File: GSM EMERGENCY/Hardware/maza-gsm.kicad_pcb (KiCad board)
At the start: 2 copper layers, 0 parts

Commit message: Added the Accelerometer in sch.
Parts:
- added AE1: Antenna, kicad_libraries:GSM_ANTENNA_Yageo_ANT2112A010B0918A, F.Cu at (17.1, 99.7)
- added BT1: Battery_Cell, Pin_Headers:Pin_Header_Straight_1x02_Pitch2.54mm, F.Cu at (32.4, 188.0)
- added C1: 10pF, Capacitors_SMD:C_0805_HandSoldering, F.Cu at (19.0, 110.9)
- added C10: 10pF, Capacitors_SMD:C_0805_HandSoldering, F.Cu at (19.3, 139.0)
- added C11: 10pF, Capacitors_SMD:C_0805_HandSoldering, F.Cu at (19.2, 141.9)
- added C12: 10pF, Capacitors_SMD:C_0805_HandSoldering, F.Cu at (19.3, 144.8)
- added C13: 470uF,E, Capacitors_SMD:CP_Elec_10x10.5, F.Cu at (70.8, 173.3)
- added C14: 33pF, Capacitors_SMD:C_0805_HandSoldering, F.Cu at (24.8, 33.7)
- added C15: 33pF, Capacitors_SMD:C_0805_HandSoldering, F.Cu at (26.0, 111.4)
- added C16: 33pF, Capacitors_SMD:C_0805_HandSoldering, F.Cu at (25.9, 113.7)
- added C17: 33pF, Capacitors_SMD:C_0805_HandSoldering, F.Cu at (26.0, 116.2)
- added C18: 33pF, Capacitors_SMD:C_0805_HandSoldering, F.Cu at (26.0, 118.9)
- added C19: 33pF, Capacitors_SMD:C_0805_HandSoldering, F.Cu at (25.9, 122.1)
- added C2: 10pF, Capacitors_SMD:C_0805_HandSoldering, F.Cu at (18.8, 113.9)
- added C20: 33pF, Capacitors_SMD:C_0805_HandSoldering, F.Cu at (25.5, 125.2)
- added C21: 33pF, Capacitors_SMD:C_0805_HandSoldering, F.Cu at (26.0, 128.8)
- added C22: 33pF, Capacitors_SMD:C_0805_HandSoldering, F.Cu at (26.1, 132.2)
- added C23: 33pF, Capacitors_SMD:C_0805_HandSoldering, F.Cu at (26.0, 136.3)
- added C24: 33pF, Capacitors_SMD:C_0805_HandSoldering, F.Cu at (26.3, 139.2)
- added C25: 33pF, Capacitors_SMD:C_0805_HandSoldering, F.Cu at (26.9, 141.7)
- added C26: 33pF, Capacitors_SMD:C_0805_HandSoldering, F.Cu at (27.3, 144.9)
- added C27: 100nF, Capacitors_SMD:C_0805_HandSoldering, F.Cu at (87.7, 192.3)
- added C28: 33pF, Capacitors_SMD:C_0805_HandSoldering, F.Cu at (31.4, 34.2)
- added C29: 33pF, Capacitors_SMD:C_0805_HandSoldering, F.Cu at (25.3, 36.9)
- added C3: 10pF, Capacitors_SMD:C_0805_HandSoldering, F.Cu at (18.6, 117.5)
- added C30: 33pF, Capacitors_SMD:C_0805_HandSoldering, F.Cu at (38.6, 19.2)
- added C31: 470uF,E, Capacitors_SMD:CP_Elec_10x10.5, F.Cu at (68.9, 185.3)
- added C32: 100nF, Capacitors_SMD:C_0805_HandSoldering, F.Cu at (84.5, 171.4)
- added C33: 100uF,Tantalum, ESR=0.7Ohm, Capacitors_Tantalum_SMD:CP_Tantalum_Case-X_EIA-7343-43_Hand, F.Cu at (90.7, 186.7)
- added C34: 100nF, Capacitors_SMD:C_0805_HandSoldering, F.Cu at (37.6, 35.8)
- added C35: 100nF, Capacitors_SMD:C_0805_HandSoldering, F.Cu at (86.9, 175.3)
- added C36: 100nF, Capacitors_SMD:C_0805_HandSoldering, F.Cu at (38.6, 15.0)
- added C37: 10pF, Capacitors_SMD:C_0805_HandSoldering, F.Cu at (86.9, 178.6)
- added C38: 33pF, Capacitors_SMD:C_0805_HandSoldering, F.Cu at (86.9, 181.3)
- added C39: 10pF, Capacitors_SMD:C_0805_HandSoldering, F.Cu at (49.7, 110.6)
- added C4: 10pF, Capacitors_SMD:C_0805_HandSoldering, F.Cu at (18.6, 119.7)
- added C40: 10pF, Capacitors_SMD:C_0805_HandSoldering, F.Cu at (50.2, 113.2)
- added C41: 10pF, Capacitors_SMD:C_0805_HandSoldering, F.Cu at (50.0, 115.8)
- added C42: 22uF, Capacitors_SMD:C_0805_HandSoldering, F.Cu at (50.0, 118.2)
- added C43: 33pF, Capacitors_SMD:C_0805_HandSoldering, F.Cu at (57.0, 110.4)
- added C44: 33pF, Capacitors_SMD:C_0805_HandSoldering, F.Cu at (57.1, 113.1)
- added C45: 33pF, Capacitors_SMD:C_0805_HandSoldering, F.Cu at (57.2, 115.8)
- added C46: 10uF, Capacitors_SMD:C_0805_HandSoldering, F.Cu at (57.6, 118.6)
- added C47: 33pF, Capacitors_SMD:C_0805_HandSoldering, F.Cu at (57.9, 121.2)
- added C48: 1uF, Capacitors_SMD:C_0805_HandSoldering, F.Cu at (155.0, 171.1)
- added C49: NM C, Capacitors_SMD:C_0805_HandSoldering, F.Cu at (27.7, 103.0)
- added C5: 10pF, Capacitors_SMD:C_0805_HandSoldering, F.Cu at (18.9, 123.7)
- added C50: NM C, Capacitors_SMD:C_0805_HandSoldering, F.Cu at (93.8, 108.6)
- added C51: NM C, Capacitors_SMD:C_0805_HandSoldering, F.Cu at (94.4, 111.7)
- added C52: 10uF, Capacitors_SMD:C_0805_HandSoldering, F.Cu at (51.8, 123.9)
- added C53: 4.7uF, Capacitors_SMD:C_0805_HandSoldering, F.Cu at (51.4, 121.0)
- added C54: 33pF, Capacitors_SMD:C_0805_HandSoldering, F.Cu at (57.6, 123.8)
- added C55: 33pF, Capacitors_SMD:C_0805_HandSoldering, F.Cu at (58.0, 32.4)
- added C56: NM C, Capacitors_SMD:C_0805_HandSoldering, F.Cu at (33.1, 103.1)
- added C57: NM C, Capacitors_SMD:C_0805_HandSoldering, F.Cu at (93.7, 105.4)
- added C58: NM C, Capacitors_SMD:C_0805_HandSoldering, F.Cu at (94.6, 115.2)
- added C59: 33pF, Capacitors_SMD:C_0805_HandSoldering, F.Cu at (63.8, 32.3)
- added C6: 10pF, Capacitors_SMD:C_0805_HandSoldering, F.Cu at (18.9, 126.5)
- added C60: 33pF, Capacitors_SMD:C_0805_HandSoldering, F.Cu at (59.2, 35.3)
- added C61: 4.7uF, Capacitors_SMD:C_0805_HandSoldering, F.Cu at (155.4, 174.7)
- added C62: 33pF, Capacitors_SMD:C_0805_HandSoldering, F.Cu at (64.3, 35.6)
- added C63: 100nF, Capacitors_SMD:C_0805_HandSoldering, F.Cu at (155.4, 178.2)
- added C64: 10uF, Capacitors_SMD:C_0805_HandSoldering, F.Cu at (155.5, 184.8)
- added C65: 100nF, Capacitors_SMD:C_0805_HandSoldering, F.Cu at (155.5, 181.6)
- added C66: 100nF, Capacitors_SMD:C_0805_HandSoldering, F.Cu at (67.9, 26.3)
- added C67: 100nF, Capacitors_SMD:C_0805_HandSoldering, F.Cu at (68.0, 29.3)
- added C68: 100uF, Capacitors_SMD:C_0805_HandSoldering, F.Cu at (16.9, 167.7)
- added C69: 4.7uF, Capacitors_SMD:C_0805_HandSoldering, F.Cu at (13.6, 167.6)
- added C7: 10pF, Capacitors_SMD:C_0805_HandSoldering, F.Cu at (19.1, 129.4)
- added C70: 100uF, Capacitors_SMD:C_0805_HandSoldering, F.Cu at (20.5, 167.7)
- added C71: 100uF, Capacitors_SMD:C_0805_HandSoldering, F.Cu at (24.6, 167.8)
- added C72: 100uF, Capacitors_SMD:C_0805_HandSoldering, F.Cu at (27.7, 167.8)
- added C73: 0.1uF, Capacitors_SMD:C_0805_HandSoldering, F.Cu at (111.3, 102.9)
- added C74: 15pF, Capacitors_SMD:C_0805_HandSoldering, F.Cu at (121.3, 105.9)
- added C75: 4.7uF, Capacitors_SMD:C_0805_HandSoldering, F.Cu at (25.7, 174.2)
- added C76: 0.1uF, Capacitors_SMD:C_0805_HandSoldering, F.Cu at (25.3, 182.4)
- added C77: 1uF, Capacitors_SMD:C_0805_HandSoldering, F.Cu at (24.7, 190.7)
- added C78: 0.15uF, Capacitors_SMD:C_0805_HandSoldering, F.Cu at (24.7, 187.6)
- added C79: 10uF, Capacitors_SMD:C_0805_HandSoldering, F.Cu at (42.9, 185.8)
- added C8: 10pF, Capacitors_SMD:C_0805_HandSoldering, F.Cu at (19.0, 132.8)
- added C80: 10uF, Capacitors_SMD:C_0805_HandSoldering, F.Cu at (36.5, 188.0)
- added C81: 0.47uF, Capacitors_SMD:C_0805_HandSoldering, F.Cu at (93.5, 140.9)
- added C82: 33uF, Capacitors_SMD:C_0805_HandSoldering, F.Cu at (93.6, 137.8)
- added C83: 47pF, Capacitors_SMD:C_0805_HandSoldering, F.Cu at (125.6, 38.2)
- added C84: 1pF, Capacitors_SMD:C_0805_HandSoldering, F.Cu at (125.5, 41.9)
- added C85: 33uF,16V, Capacitors_SMD:CP_Elec_3x5.3, F.Cu at (115.0, 42.1)
- added C86: CP10uF,Tantalum, ESR=0.7Ohm, Capacitors_Tantalum_SMD:CP_Tantalum_Case-A_EIA-3216-18_Hand, F.Cu at (132.4, 79.6)
- added C87: 33uF,16V,E, Capacitors_SMD:CP_Elec_3x5.3, F.Cu at (113.6, 34.8)
- added C88: 4.7uF,16V,E, Capacitors_SMD:CP_Elec_4x5.3, F.Cu at (106.1, 17.7)
- added C89: 4.7uF, Capacitors_SMD:C_0805_HandSoldering, F.Cu at (112.4, 16.3)
- added C9: 10pF, Capacitors_SMD:C_0805_HandSoldering, F.Cu at (19.3, 136.5)
- added C90: 4.7uF, Capacitors_SMD:C_0805_HandSoldering, F.Cu at (112.3, 19.9)
- added C91: 10uF,16V,E, Capacitors_SMD:CP_Elec_5x5.3, F.Cu at (104.4, 26.3)
- added D1: TVS_DIODE_CM1224, kicad_libraries:CM1224-4SO-SOT23, F.Cu at (19.5, 35.8)
- added D10: TVS_DIODE_CM1224, kicad_libraries:CM1224-4SO-SOT23, F.Cu at (51.7, 33.3)
- added D11: D_TVS_ALT, Diodes_SMD:D_SOD-123, F.Cu at (63.3, 122.3)
- added D12: SS14FL, kicad_libraries:SChottky-diode-SS14FL-Fairchild, F.Cu at (107.1, 31.9)
- added D2: ESD, Diodes_SMD:D_SOD-123, F.Cu at (35.3, 119.3)
- added D3: ESD, Diodes_SMD:D_SOD-123, F.Cu at (35.4, 122.7)
- added D4: ESD, Diodes_SMD:D_SOD-123, F.Cu at (35.7, 126.2)
- added D5: ESD, Diodes_SMD:D_SOD-123, F.Cu at (36.1, 129.9)
- added D6: ESD, Diodes_SMD:D_SOD-123, F.Cu at (35.9, 133.6)
- added D7: ESD, Diodes_SMD:D_SOD-123, F.Cu at (36.0, 137.2)
- added D8: 5.1V Zener, Diodes_SMD:D_SOD-123, F.Cu at (93.3, 175.9)
- added D9: D_TVS_ALT, Diodes_SMD:D_SOD-123, F.Cu at (50.1, 130.1)
- added F1: IPEX_CON, kicad_libraries:IPEX_CON_MHF, F.Cu at (87.7, 112.3)
- added F2: IPEX_CON, kicad_libraries:IPEX_CON_MHF, F.Cu at (82.2, 112.2)
- added J1: SIM_Card, kicad_libraries:MICRO-SIM-78646-3001-MOLEX, F.Cu at (30.7, 29.3)
- added J10: ON_OFF_SWITCH, Connectors_Terminal_Blocks:TerminalBlock_Pheonix_MPT-2.54mm_3pol, F.Cu at (33.7, 172.9)
- added J11: LED2, Connectors_Terminal_Blocks:TerminalBlock_Pheonix_MPT-2.54mm_2pol, F.Cu at (106.2, 125.1)
- added J12: LED3, Connectors_Terminal_Blocks:TerminalBlock_Pheonix_MPT-2.54mm_2pol, F.Cu at (106.3, 137.0)
- added J13: LED4, Connectors_Terminal_Blocks:TerminalBlock_Pheonix_MPT-2.54mm_2pol, F.Cu at (106.5, 148.2)
- added J14: LED5, Connectors_Terminal_Blocks:TerminalBlock_Pheonix_MPT-2.54mm_2pol, F.Cu at (107.3, 159.1)
- added J15: LED6, Connectors_Terminal_Blocks:TerminalBlock_Pheonix_MPT-2.54mm_2pol, F.Cu at (107.3, 169.3)
- added J16: LED7, Connectors_Terminal_Blocks:TerminalBlock_Pheonix_MPT-2.54mm_2pol, F.Cu at (107.7, 180.2)
- added J17: LED8, Connectors_Terminal_Blocks:TerminalBlock_Pheonix_MPT-2.54mm_2pol, F.Cu at (109.0, 190.3)
- added J18: OLED CONNECTOR, Connectors_Molex:Molex_Panelmate-53780-3070_30x1.25mm_Angled, F.Cu at (142.0, 37.3)
- added J19: PB1, Pin_Headers:Pin_Header_Straight_1x02_Pitch2.54mm, F.Cu at (93.2, 17.9)
- added J2: NETWORK_LED, Connectors_Terminal_Blocks:TerminalBlock_Pheonix_MPT-2.54mm_2pol, F.Cu at (34.1, 52.6)
- added J20: PB2, Pin_Headers:Pin_Header_Straight_1x02_Pitch2.54mm, F.Cu at (86.7, 17.9)
- added J21: PB3, Pin_Headers:Pin_Header_Straight_1x02_Pitch2.54mm, F.Cu at (82.2, 17.3)
- added J22: PB4, Pin_Headers:Pin_Header_Straight_1x02_Pitch2.54mm, F.Cu at (77.5, 17.5)
- added J23: OLED_INDICATOR, Pin_Headers:Pin_Header_Straight_1x02_Pitch2.54mm, F.Cu at (127.1, 17.9)
- added J24: 32Ohm,Speaker, Pin_Headers:Pin_Header_Straight_1x02_Pitch2.54mm, F.Cu at (41.1, 120.0)
- added J25: 8OHM, SPEAKER, Pin_Headers:Pin_Header_Straight_1x02_Pitch2.54mm, F.Cu at (41.3, 130.0)
- added J26: 2.2Kohms, Load Res.Mic, Pin_Headers:Pin_Header_Straight_1x02_Pitch2.54mm, F.Cu at (41.1, 138.8)
- added J27: ICSP, Pin_Headers:Pin_Header_Straight_1x05_Pitch2.54mm, F.Cu at (99.2, 80.8)
- added J3: PCM CON, Pin_Headers:Pin_Header_Straight_1x04_Pitch2.54mm, F.Cu at (19.7, 73.4)
- added J4: SD CON, Pin_Headers:Pin_Header_Straight_1x03_Pitch2.54mm, F.Cu at (40.3, 69.2)
- added J5: 1PPS_LED, Connectors_Terminal_Blocks:TerminalBlock_Pheonix_MPT-2.54mm_2pol, F.Cu at (67.7, 86.0)
- added J6: SIM_Card, kicad_libraries:MICRO-SIM-78646-3001-MOLEX, F.Cu at (63.2, 27.9)
- added J7: USB_OTG, Connectors:USB_Micro-B_10103594-0001LF, F.Cu at (16.9, 189.2)
- added J8: POWER_ADAPTER, Connectors_Terminal_Blocks:TerminalBlock_Pheonix_MPT-2.54mm_2pol, F.Cu at (16.2, 178.5)
- added J9: LED1, Connectors_Terminal_Blocks:TerminalBlock_Pheonix_MPT-2.54mm_2pol, F.Cu at (110.0, 119.0)
- added L1: 1uH, Inductors_SMD:L_0805_HandSoldering, F.Cu at (42.4, 181.5)
- added L2: 18uH, Inductors_SMD:L_0805_HandSoldering, F.Cu at (106.5, 35.9)
- added Q1: BC847, TO_SOT_Packages_SMD:SOT-23_Handsoldering, F.Cu at (27.0, 54.6)
- added Q10: BC847, TO_SOT_Packages_SMD:SOT-23_Handsoldering, F.Cu at (124.0, 53.0)
- added Q11: BC847, TO_SOT_Packages_SMD:SOT-23_Handsoldering, F.Cu at (117.0, 167.8)
- added Q12: BC847, TO_SOT_Packages_SMD:SOT-23_Handsoldering, F.Cu at (116.2, 179.2)
- added Q13: BC847, TO_SOT_Packages_SMD:SOT-23_Handsoldering, F.Cu at (116.5, 191.1)
- added Q2: BC847, TO_SOT_Packages_SMD:SOT-23_Handsoldering, F.Cu at (81.0, 176.4)
- added Q3: BC857, TO_SOT_Packages_SMD:SOT-23_Handsoldering, F.Cu at (54.9, 87.9)
- added Q4: BC847, TO_SOT_Packages_SMD:SOT-23_Handsoldering, F.Cu at (90.3, 151.0)
- added Q5: BC847, TO_SOT_Packages_SMD:SOT-23_Handsoldering, F.Cu at (117.8, 117.0)
- added Q6: BC847, TO_SOT_Packages_SMD:SOT-23_Handsoldering, F.Cu at (117.5, 126.9)
- added Q7: BC847, TO_SOT_Packages_SMD:SOT-23_Handsoldering, F.Cu at (118.0, 136.1)
- added Q8: BC847, TO_SOT_Packages_SMD:SOT-23_Handsoldering, F.Cu at (117.7, 146.8)
- added Q9: BC847, TO_SOT_Packages_SMD:SOT-23_Handsoldering, F.Cu at (117.2, 158.8)
- added R1: 0R, Resistors_SMD:R_0805_HandSoldering, F.Cu at (31.5, 111.8)
- added R10: 300R, Resistors_SMD:R_0805_HandSoldering, F.Cu at (22.2, 52.4)
- added R11: 0R, Resistors_SMD:R_0805_HandSoldering, F.Cu at (35.3, 141.0)
- added R12: 0R, Resistors_SMD:R_0805_HandSoldering, F.Cu at (34.6, 144.6)
- added R13: 124K, Resistors_SMD:R_0805_HandSoldering, F.Cu at (78.1, 189.6)
- added R14: 56K, Resistors_SMD:R_0805_HandSoldering, F.Cu at (78.1, 183.3)
- added R15: 470R, Resistors_SMD:R_0805_HandSoldering, F.Cu at (77.6, 186.4)
- added R16: 22R, Resistors_SMD:R_0805_HandSoldering, F.Cu at (38.0, 31.1)
- added R17: 22R, Resistors_SMD:R_0805_HandSoldering, F.Cu at (38.1, 27.3)
- added R18: 22R, Resistors_SMD:R_0805_HandSoldering, F.Cu at (38.1, 23.5)
- added R19: 4.7K, Resistors_SMD:R_0805_HandSoldering, F.Cu at (60.6, 83.1)
- added R2: 0R, Resistors_SMD:R_0805_HandSoldering, F.Cu at (32.2, 114.7)
- added R20: 0R, Resistors_SMD:R_0805_HandSoldering, F.Cu at (63.0, 109.9)
- added R21: 0R, Resistors_SMD:R_0805_HandSoldering, F.Cu at (62.9, 113.3)
- added R22: 0R, Resistors_SMD:R_0805_HandSoldering, F.Cu at (63.0, 116.3)
- added R23: 47K, Resistors_SMD:R_0805_HandSoldering, F.Cu at (60.8, 86.8)
- added R24: 300R, Resistors_SMD:R_0805_HandSoldering, F.Cu at (61.2, 91.0)
- added R25: 0R, Resistors_SMD:R_0805_HandSoldering, F.Cu at (73.6, 55.2)
- added R26: 0R, Resistors_SMD:R_0805_HandSoldering, F.Cu at (72.9, 59.1)
- added R27: 47K, Resistors_SMD:R_0805_HandSoldering, F.Cu at (162.4, 174.8)
- added R28: 0R, Resistors_SMD:R_0805_HandSoldering, F.Cu at (20.4, 102.8)
- added R29: 0R, Resistors_SMD:R_0805_HandSoldering, F.Cu at (82.4, 106.9)
- added R3: 4.7K, Resistors_SMD:R_0805_HandSoldering, F.Cu at (21.9, 49.4)
- added R30: 0R, Resistors_SMD:R_0805_HandSoldering, F.Cu at (88.3, 106.7)
- added R31: 1K, Resistors_SMD:R_0805_HandSoldering, F.Cu at (73.0, 64.6)
- added R32: 1K, Resistors_SMD:R_0805_HandSoldering, F.Cu at (73.0, 67.4)
- added R33: 1K, Resistors_SMD:R_0805_HandSoldering, F.Cu at (73.1, 69.8)
- added R34: 1K, Resistors_SMD:R_0805_HandSoldering, F.Cu at (73.5, 72.4)
- added R35: 5.6K, Resistors_SMD:R_0805_HandSoldering, F.Cu at (73.9, 61.6)
- added R36: 75K, 1%, Resistors_SMD:R_0805_HandSoldering, F.Cu at (162.7, 178.8)
- added R37: 43K, 1%, Resistors_SMD:R_0805_HandSoldering, F.Cu at (162.6, 183.1)
- added R38: 22R, Resistors_SMD:R_0805_HandSoldering, F.Cu at (68.1, 23.5)
- added R39: 22R, Resistors_SMD:R_0805_HandSoldering, F.Cu at (67.5, 19.5)
- added R4: 4.7K, Resistors_SMD:R_0805_HandSoldering, F.Cu at (96.0, 191.5)
- added R40: 22R, Resistors_SMD:R_0805_HandSoldering, F.Cu at (67.3, 15.5)
- added R41: 4.7K, Resistors_SMD:R_0805_HandSoldering, F.Cu at (91.8, 155.6)
- added R42: 47K, Resistors_SMD:R_0805_HandSoldering, F.Cu at (95.8, 150.8)
- added R43: 10K, Resistors_SMD:R_0805_HandSoldering, F.Cu at (89.1, 24.3)
- added R44: 0R, Resistors_SMD:R_0805_HandSoldering, F.Cu at (82.8, 25.8)
- added R45: 10K, Resistors_SMD:R_0805_HandSoldering, F.Cu at (88.5, 28.3)
- added R46: 10K, Resistors_SMD:R_0805_HandSoldering, F.Cu at (111.4, 99.0)
- added R47: 0R, Resistors_SMD:R_0805_HandSoldering, F.Cu at (25.3, 178.5)
- added R48: 0R, Resistors_SMD:R_0805_HandSoldering, F.Cu at (81.7, 29.6)
- added R49: 10K, Resistors_SMD:R_0805_HandSoldering, F.Cu at (81.5, 33.1)
- added R5: 47K, Resistors_SMD:R_0805_HandSoldering, F.Cu at (96.5, 195.5)
- added R50: 0R, Resistors_SMD:R_0805_HandSoldering, F.Cu at (82.0, 36.4)
- added R51: 100K, Resistors_SMD:R_0805_HandSoldering, F.Cu at (43.1, 189.5)
- added R52: 100K, Resistors_SMD:R_0805_HandSoldering, F.Cu at (37.5, 184.1)
- added R53: 10K, Resistors_SMD:R_0805_HandSoldering, F.Cu at (88.2, 32.7)
- added R54: 3K, Resistors_SMD:R_0805_HandSoldering, F.Cu at (38.7, 178.7)
- added R55: 0R, Resistors_SMD:R_0805_HandSoldering, F.Cu at (88.8, 36.9)
- added R56: 1.2K, Resistors_SMD:R_0805_HandSoldering, F.Cu at (39.0, 192.3)
- added R57: 100K, Resistors_SMD:R_0805_HandSoldering, F.Cu at (42.4, 178.0)
- added R58: 4.7K, Resistors_SMD:R_0805_HandSoldering, F.Cu at (121.3, 117.0)
- added R59: 100K, Resistors_SMD:R_0805_HandSoldering, F.Cu at (42.0, 174.2)
- added R6: 0R, Resistors_SMD:R_0805_HandSoldering, F.Cu at (40.1, 111.7)
- added R60: 47K, Resistors_SMD:R_0805_HandSoldering, F.Cu at (128.9, 117.0)
- added R61: 300R, Resistors_SMD:R_0805_HandSoldering, F.Cu at (124.6, 117.2)
- added R62: 4.7K, Resistors_SMD:R_0805_HandSoldering, F.Cu at (125.0, 127.7)
- added R63: 47K, Resistors_SMD:R_0805_HandSoldering, F.Cu at (128.3, 127.0)
- added R64: 300R, Resistors_SMD:R_0805_HandSoldering, F.Cu at (121.9, 126.7)
- added R65: 4.7K, Resistors_SMD:R_0805_HandSoldering, F.Cu at (121.7, 136.1)
- added R66: 47K, Resistors_SMD:R_0805_HandSoldering, F.Cu at (125.0, 136.4)
- added R67: 300R, Resistors_SMD:R_0805_HandSoldering, F.Cu at (128.7, 136.7)
- added R68: 4.7K, Resistors_SMD:R_0805_HandSoldering, F.Cu at (122.0, 146.7)
- added R69: 10K, Resistors_SMD:R_0805_HandSoldering, F.Cu at (119.6, 31.6)
- added R7: 0R, Resistors_SMD:R_0805_HandSoldering, F.Cu at (40.1, 114.5)
- added R70: 47K, Resistors_SMD:R_0805_HandSoldering, F.Cu at (124.9, 147.1)
- added R71: 300R, Resistors_SMD:R_0805_HandSoldering, F.Cu at (129.4, 146.8)
- added R72: 4.7K, Resistors_SMD:R_0805_HandSoldering, F.Cu at (125.2, 160.3)
- added R73: 47K, Resistors_SMD:R_0805_HandSoldering, F.Cu at (129.1, 159.9)
- added R74: 4.7K, Resistors_SMD:R_0805_HandSoldering, F.Cu at (128.4, 46.2)
- added R75: 300R, Resistors_SMD:R_0805_HandSoldering, F.Cu at (122.0, 159.7)
- added R76: 300R, Resistors_SMD:R_0805_HandSoldering, F.Cu at (123.5, 46.5)
- added R77: 4.7K, Resistors_SMD:R_0805_HandSoldering, F.Cu at (121.4, 168.6)
- added R78: 47K, Resistors_SMD:R_0805_HandSoldering, F.Cu at (124.8, 168.3)
- added R79: 300R, Resistors_SMD:R_0805_HandSoldering, F.Cu at (129.2, 169.0)
- added R8: 51K, Resistors_SMD:R_0805_HandSoldering, F.Cu at (90.5, 195.8)
- added R80: 3K3, Resistors_SMD:R_0805_HandSoldering, F.Cu at (131.9, 20.6)
- added R81: 4.7K, Resistors_SMD:R_0805_HandSoldering, F.Cu at (120.8, 179.0)
- added R82: 47K, Resistors_SMD:R_0805_HandSoldering, F.Cu at (124.0, 179.1)
- added R83: 300R, Resistors_SMD:R_0805_HandSoldering, F.Cu at (128.0, 179.4)
- added R84: 0R, Resistors_SMD:R_0805_HandSoldering, F.Cu at (128.4, 85.5)
- added R85: 4.7K, Resistors_SMD:R_0805_HandSoldering, F.Cu at (121.2, 190.9)
- added R86: 820K, Resistors_SMD:R_0805_HandSoldering, F.Cu at (112.7, 31.1)
- added R87: 47K, Resistors_SMD:R_0805_HandSoldering, F.Cu at (125.6, 191.1)
- added R88: 0R, Resistors_SMD:R_0805_HandSoldering, F.Cu at (133.8, 84.1)
- added R89: 300R, Resistors_SMD:R_0805_HandSoldering, F.Cu at (130.0, 190.9)
- added R9: 47K, Resistors_SMD:R_0805_HandSoldering, F.Cu at (28.3, 49.8)
- added U1: MIC29302_LDO, TO_SOT_Packages_SMD:TO-263-5Lead, F.Cu at (56.5, 179.8)
- added U2: MC60, kicad_libraries:MC60-Quectel, F.Cu at (59.2, 62.3)
- added U3: SGM2019_LDO, TO_SOT_Packages_SMD:SOT-23-5_HandSoldering, F.Cu at (149.7, 178.2)
- added U4: Audio_Jack3.5mm, kicad_libraries:Audio_Jack_3.5mm, F.Cu at (57.6, 130.4)
- added U4: Audio_Jack3.5mm, kicad_libraries:Audio_Jack_3.5mm, F.Cu at (57.9, 130.0)
- added U5: MAX8903A, Housings_DFN_QFN:QFN-28-1EP_4x4mm_Pitch0.4mm, F.Cu at (33.2, 179.8)
- added U6: LM3940, TO_SOT_Packages_SMD:SOT-223, F.Cu at (93.4, 131.0)
- added U7: PIC32MX440F512H, kicad_libraries:TQFP_64-10mmX10mm, F.Cu at (115.8, 82.4)
- added U8: MAX734, kicad_libraries:SO-8, F.Cu at (120.1, 17.7)
- added X1: oscillator_DSC1033, kicad_libraries:OSC_DS1033, F.Cu at (121.9, 99.3)
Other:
- board text added: "1PPS LED CIRCUIT"
- board text added: "3.3 V REGULATOR"
- board text added: "AUDIO CIRCUIT"
- board text added: "BT ANTENNA CIRCUIT GNSS ANTENNA CIRCUIT"
- board text added: "CHARGING CIRCUIT"
- board text added: "DIGITAL AUDIO (PCM) INTERFACE"
- board text added: "EarPhone Interface"
- board text added: "GPP LED CIRCUIT"
- board text added: "NETWORK LED CIRCUIT"
- board text added: "OLED DISPLAY INTERFACE"
- board text added: "POWER SWITCH FOR GSM MODULE"
- board text added: "PUSH BUTTON INTERFACE"
- board text added: "Power Supply of the GSM Part"
- board text added: "Power supply of GNSS Part in All-in-one Solution"
- board text added: "RESET CKT"
- board text added: "RF ANTENNA CIRCUIT"
- board text added: "SD CARD INTERFACE"
- board text added: "SIM CARD INTERFACE"
- board text added: "SIM2 CARD INTERFACE"

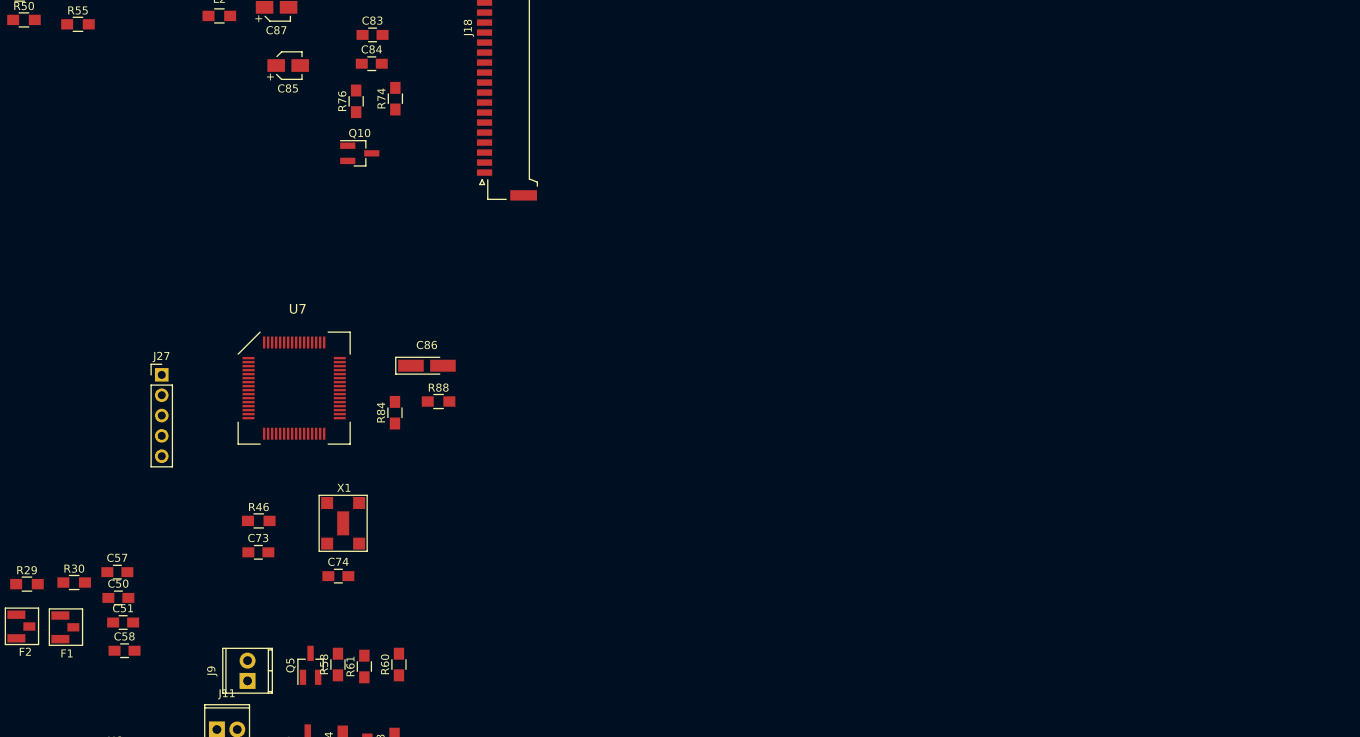
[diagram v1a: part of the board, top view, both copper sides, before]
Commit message: Loaded netlist to pcbnew and sorted components, added pcb keepout
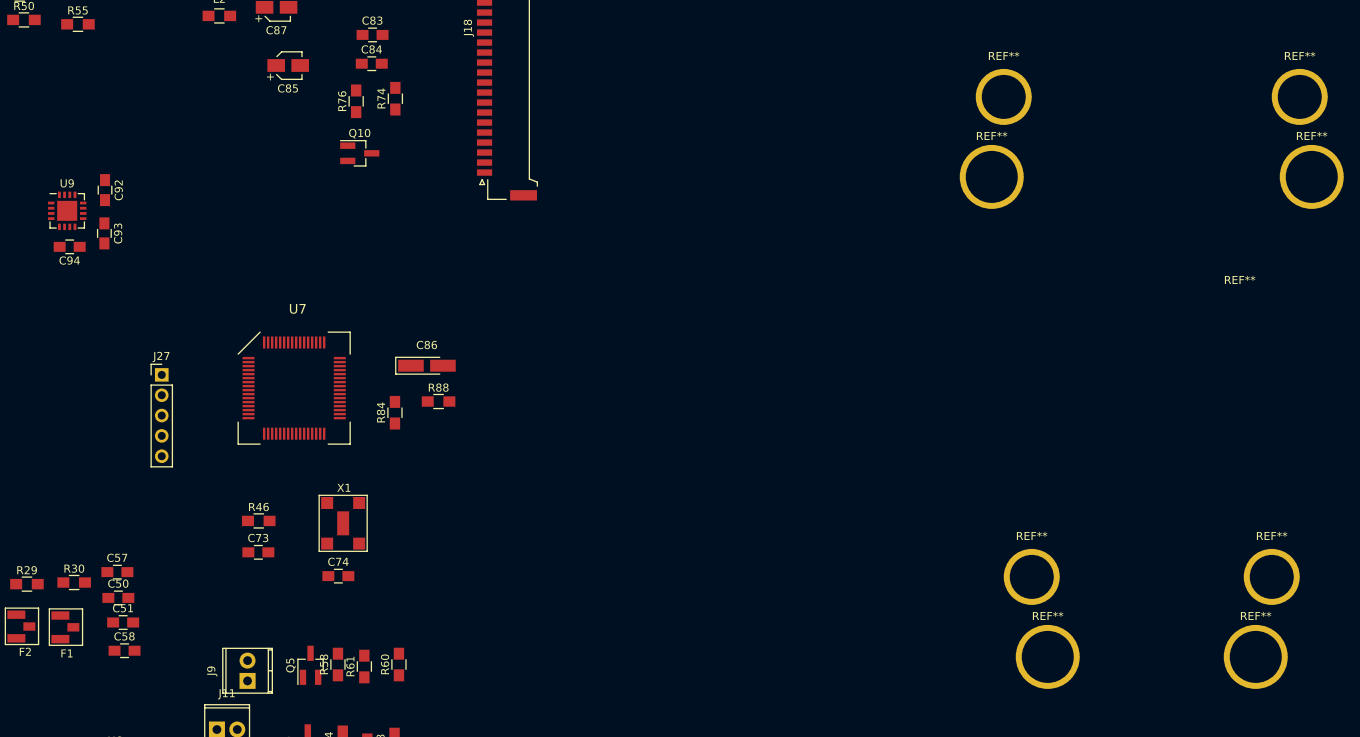
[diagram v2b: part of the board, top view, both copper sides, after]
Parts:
- added C92: 0.1uF, Capacitors_SMD:C_0805_HandSoldering, F.Cu at (92.2, 57.6)
- added C93: 0.1uF, Capacitors_SMD:C_0805_HandSoldering, F.Cu at (92.1, 63.1)
- added C94: 0.1uF, Capacitors_SMD:C_0805_HandSoldering, F.Cu at (87.7, 64.7)
- added REF**: SolderWirePad_single_2-5mmDrill, Wire_Pads:SolderWirePad_single_2-5mmDrill, F.Cu at (234.0, 74.0)
- added REF**: SolderWirePad_single_2-5mmDrill, Wire_Pads:SolderWirePad_single_2-5mmDrill, F.Cu at (204.5, 46.0)
- added REF**: SolderWirePad_single_2-5mmDrill, Wire_Pads:SolderWirePad_single_2-5mmDrill, F.Cu at (243.0, 56.0)
- added REF**: SolderWirePad_single_2-5mmDrill, Wire_Pads:SolderWirePad_single_2-5mmDrill, F.Cu at (241.5, 46.0)
- added REF**: SolderWirePad_single_2-5mmDrill, Wire_Pads:SolderWirePad_single_2-5mmDrill, F.Cu at (203.0, 56.0)
- added REF**: SolderWirePad_single_2-5mmDrill, Wire_Pads:SolderWirePad_single_2-5mmDrill, F.Cu at (210.0, 116.0)
- added REF**: SolderWirePad_single_2-5mmDrill, Wire_Pads:SolderWirePad_single_2-5mmDrill, F.Cu at (208.0, 106.0)
- added REF**: SolderWirePad_single_2-5mmDrill, Wire_Pads:SolderWirePad_single_2-5mmDrill, F.Cu at (238.0, 106.0)
- added REF**: SolderWirePad_single_2-5mmDrill, Wire_Pads:SolderWirePad_single_2-5mmDrill, F.Cu at (236.0, 116.0)
- added U9: ADXL_335, Housings_DFN_QFN:QFN-16-1EP_4x4mm_Pitch0.65mm, F.Cu at (87.4, 60.2)
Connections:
- U7 pad 13: OLED_VDD -> ST
- U7 pad 14: OLED_RST -> ZOUT
- U7 pad 15: OLED_D/C -> YOUT
- U7 pad 16: OLED_SCK -> XOUT
- U7 pad 49: (no net) -> OLED_VDD
- U7 pad 52: (no net) -> OLED_RST
- U7 pad 55: (no net) -> OLED_D/C
- U7 pad 60: (no net) -> OLED_SCK
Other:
- board text added: "ACCELEROMETER"

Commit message: PCB completed
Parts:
- removed REF** (x9): SolderWirePad_single_2-5mmDrill, Wire_Pads:SolderWirePad_single_2-5mmDrill
- added P1: TH_PAD, kicad_libraries:TH_HOLE_PAD_5.5mm, F.Cu at (203.0, 56.0)
- added P2: TH_PAD, kicad_libraries:TH_HOLE_PAD_5.5mm, F.Cu at (208.0, 106.0)
- added P3: TH_PAD, kicad_libraries:TH_HOLE_PAD_5.5mm, F.Cu at (243.0, 56.0)
- added P4: TH_PAD, kicad_libraries:TH_HOLE_PAD_5.5mm, F.Cu at (238.0, 106.0)
- added P5: TH_PAD, kicad_libraries:TH_HOLE_PAD_6.5mm, F.Cu at (210.0, 116.0)
- added P6: TH_PAD, kicad_libraries:TH_HOLE_PAD_6.5mm, F.Cu at (241.5, 46.0)
- added P7: TH_PAD, kicad_libraries:TH_HOLE_PAD_6.5mm, F.Cu at (204.5, 46.0)
- added P8: TH_PAD, kicad_libraries:TH_HOLE_PAD_6.5mm, F.Cu at (236.0, 116.0)
- BT1: footprint Pin_Headers:Pin_Header_Straight_1x02_Pitch2.54mm -> kicad_libraries:BATTERTY_PAD_SMD
- J10: footprint Connectors_Terminal_Blocks:TerminalBlock_Pheonix_MPT-2.54mm_3pol -> kicad_libraries:SMD_2PIN_SWITCH
- J11, J12, J13, J14, J15, J16, J17, J9: footprint Connectors_Terminal_Blocks:TerminalBlock_Pheonix_MPT-2.54mm_2pol -> Resistors_SMD:R_0805_HandSoldering
- J19, J20, J21, J22: footprint Pin_Headers:Pin_Header_Straight_1x02_Pitch2.54mm -> Resistors_SMD:R_0805_HandSoldering
- J8: footprint Connectors_Terminal_Blocks:TerminalBlock_Pheonix_MPT-2.54mm_2pol -> kicad_libraries:BATTERTY_PAD_SMD
- moved BT1 231.7 mm to (220.0, 52.0)
- moved J10 18.2 mm to (16.0, 177.0)
- moved J22 15.5 mm to (78.0, 33.0), turned to 90 degrees
- moved J21 10.5 mm to (78.0, 27.0), turned to 90 degrees
- moved C81 9.82 mm to (84.0, 143.4)
- moved C82 9.82 mm to (84.1, 140.3)
- moved Q4 9.82 mm to (80.8, 153.5)
- moved R41 9.82 mm to (82.2, 158.1)
- moved R42 9.82 mm to (86.2, 153.3)
- moved U6 9.82 mm to (83.9, 133.5)
- moved J20 8.03 mm to (79.5, 21.5)
- moved J19 6.98 mm to (86.5, 20.0)
- moved C68 6.08 mm to (22.9, 166.7)
- moved C69 6.08 mm to (19.6, 166.6)
- moved C70 6.08 mm to (26.5, 166.7)
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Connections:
- J8 pad 1: GND -> USB_ADAPTER
- J8 pad 2: USB_ADAPTER -> GND
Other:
- net class Default: clearance 0.2 -> 0.1
- net class GND added: clearance 0.3, trace_width 1, via_dia 1.25, via_drill 1
- rule trace_clearance: 0.2 -> 0.1
